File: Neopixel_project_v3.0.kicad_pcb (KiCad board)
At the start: 2 copper layers, 50 x 50 mm, 64 parts, among them J1 Conn_01x03_Pin, J2 Conn_01x02_Pin, Q1 MMBT3904, Q2 MMBT3904, Q3 MMBT3904, Q4 MMBT3904, Q5 DO3407B, Q6 DO3407B, Q7 DO3407B, Q8 DO3407B, SW1 TS-1088-AR02016, SW2 TS-1088-AR02016, U1 ESP8685H4, U2 AL8843, U3 TD1469, U4 USBLC6-4SC6, Y1 Crystal_GND24

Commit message: pcb finished
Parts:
- moved SW1 40.0 mm to (215.7, 127.2)
- moved R10 38.4 mm to (217.4, 124.8)
- moved SW2 35.2 mm to (200.8, 118.5), turned to 0 degrees
- moved C12 32.4 mm to (221.8, 130.5), turned to -90 degrees
- moved C11 31.1 mm to (205.5, 118.2)
- moved R3 27.7 mm to (202.0, 123.8), turned to -90 degrees
- moved R1 23.9 mm to (199.8, 123.7), turned to -90 degrees
- moved C18 22.2 mm to (214.3, 148.2), turned to 180 degrees
- moved C4 22.2 mm to (216.8, 149.2), turned to 0 degrees
- moved R9 21.8 mm to (214.3, 123.2), turned to 0 degrees
- moved Y1 21.7 mm to (214.3, 145.6), turned to 90 degrees
- moved R12 21.6 mm to (210.7, 124.2), turned to 180 degrees
- moved C17 21.6 mm to (214.5, 143.0), turned to 0 degrees
- moved AE1 21.5 mm to (218.8, 145.4), turned to -90 degrees
- moved J1 20.0 mm to (210.8, 121.0), turned to -90 degrees
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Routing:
- net CTRL: track 0.00 -> 58.5 mm, vias 0 -> 2
- net 3v3: track 36.4 -> 81.3 mm, vias 0 -> 11
- net PWM_B: track 0.00 -> 39.3 mm, vias 0 -> 2
- net PWM_G: track 0.00 -> 33.0 mm, vias 0 -> 2
- net PWM_W: track 0.00 -> 31.8 mm, vias 0 -> 2
- net CHIP_EN: track 0.00 -> 31.3 mm, vias 0 -> 2
- net GND: track 25.9 -> 55.7 mm, vias 10 -> 18
- net USB_D+: track 0.00 -> 26.6 mm
- net USB_D-: track 0.00 -> 24.2 mm
- net PWM_R: track 0.00 -> 22.2 mm, vias 0 -> 2
- net BOOT: track 0.00 -> 20.6 mm, vias 0 -> 2
- net Net-(U1A-GPIO2): track 0.00 -> 14.2 mm, vias 0 -> 2
- net OSC_N: track 0.00 -> 13.7 mm
- net Net-(U1A-GPIO8): track 0.00 -> 11.4 mm, vias 0 -> 2
- net Net-(Q2-C): track 4.91 -> 11.7 mm
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- added copper zone on F.Cu, net 3v3
- removed copper zone on F.Cu, net GND
- removed copper zone on F.Cu, net LNA_IN
- removed copper zone on F.Cu, net Net-(AE1-A)

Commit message: pcb and 3d models finished
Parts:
- removed J2: Conn_01x02_Pin, Connector_AMASS:AMASS_XT30UPB-M_1x02_P5.0mm_Vertical
- added J3: Screw_Terminal_01x02, TerminalBlock_Phoenix:TerminalBlock_Phoenix_MPT-0,5-2-2.54_1x02_P2.54mm_Horizontal, F.Cu at (195.5, 122.7)
- moved D5 0.40 mm to (186.0, 149.1)
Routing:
- net GND: track 55.7 -> 53.2 mm, vias 18 -> 17
- net PWM_G: track 33.0 -> 32.2 mm

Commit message: added bom.csv and buch of other changes
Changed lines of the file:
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@@
 		(tags "SOT TO_SOT_SMD")
 		(property "Reference" "Q4"
-			(at 0 -2.4 180)
+			(at -0.1125 -0.05 180)
 			(layer "F.SilkS")
 			(effects
@@
 		(tags "SOT TO_SOT_SMD")
 		(property "Reference" "Q8"
-			(at 0 -2.4 0)
+			(at -0.1 -0.3 0)
 			(layer "F.SilkS")
 			(effects
@@
 		(tags "Diode SMA (DO-214AC)")
 		(property "Reference" "D5"
-			(at 0 -2.5 180)
+			(at 0.025 -0.1 180)
 			(layer "F.SilkS")
 			(effects
@@
 		(tags "resistor")
 		(property "Reference" "R7"
-			(at 0 -1.82 90)
+			(at -0.1375 -0.1 90)
 			(layer "F.SilkS")
 			(effects
@@
 		(tags "resistor")
 		(property "Reference" "R15"
-			(at 0 -1.43 270)
+			(at 0 0.05 270)
 			(layer "F.SilkS")
 			(effects
@@
 		(tags "smd inductor dlg-0504")
 		(property "Reference" "L1"
-			(at 0 -3.7 180)
+			(at 0 -0.05 180)
 			(layer "F.SilkS")
 			(effects
@@
 		(tags "capacitor electrolytic")
 		(property "Reference" "C2"
-			(at 0 -4.35 360)
+			(at -0.05 0 360)
 			(layer "F.SilkS")
 			(effects
@@
 		(layer "User.1")
 	)
-	(gr_circle
-		(center 201 141)
-		(end 228.5 141)
-		(stroke
-			(width 0.1)
-			(type default)
-		)
-		(fill none)
-		(layer "User.2")
-	)
 	(dimension

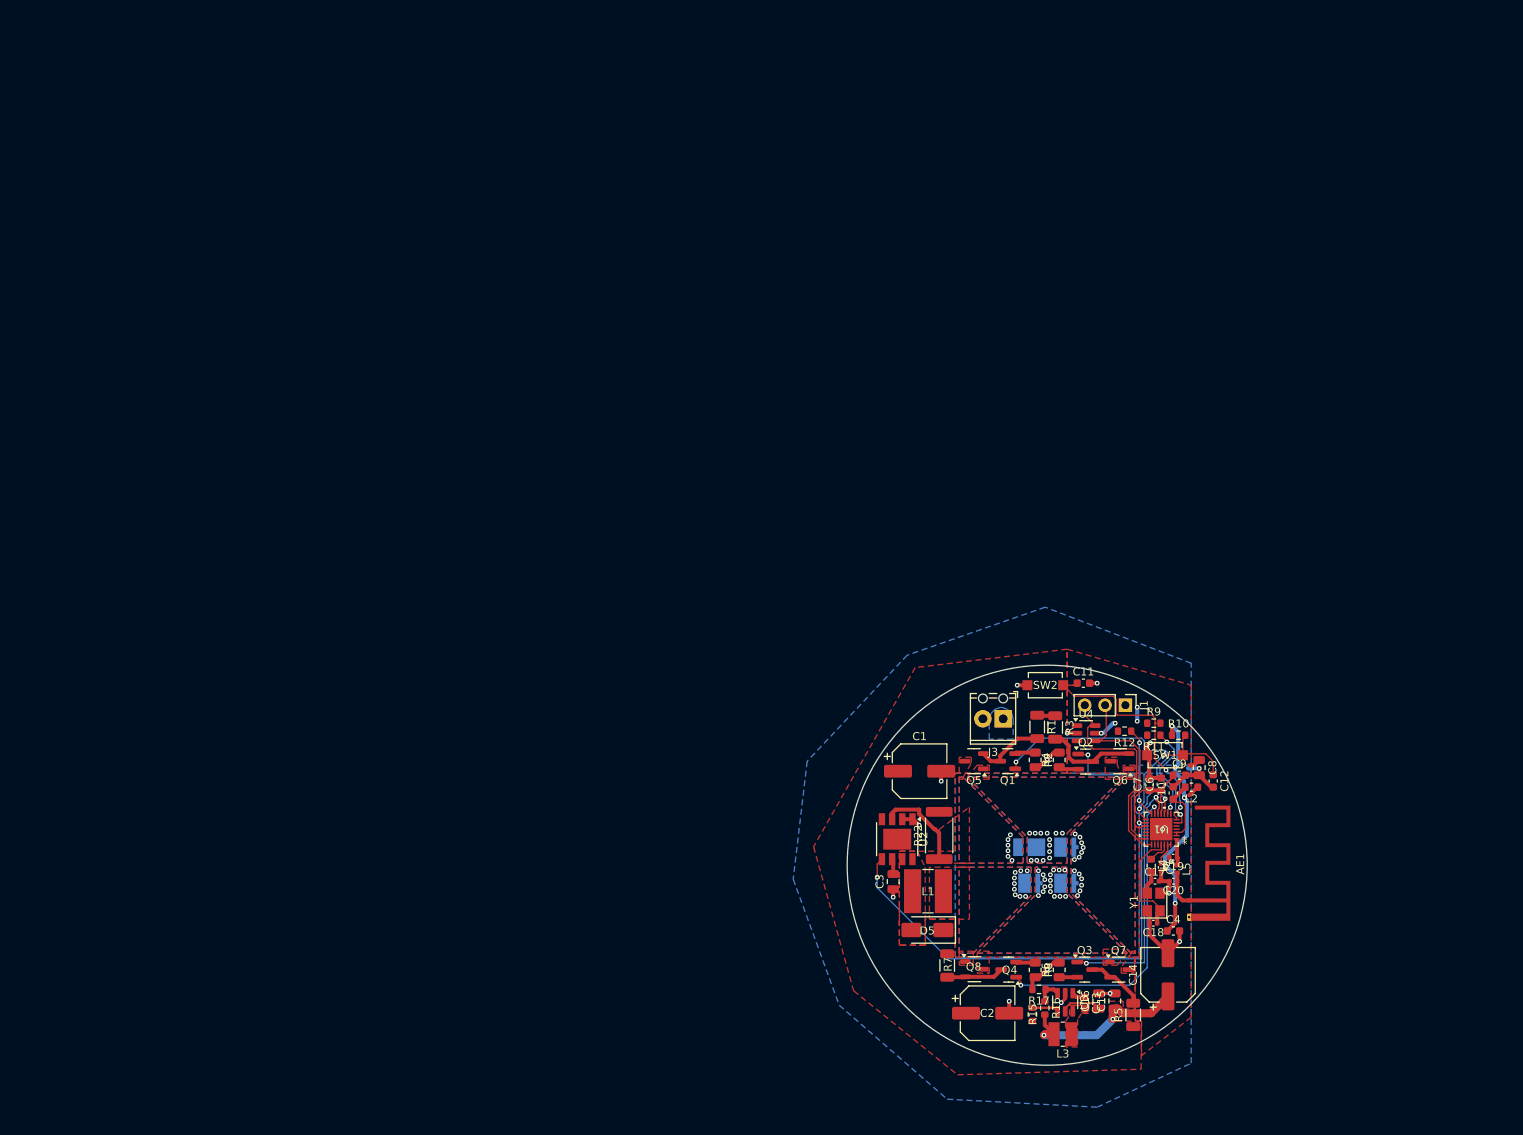
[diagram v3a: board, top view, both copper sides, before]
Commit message: silkscreen removed and layout printed
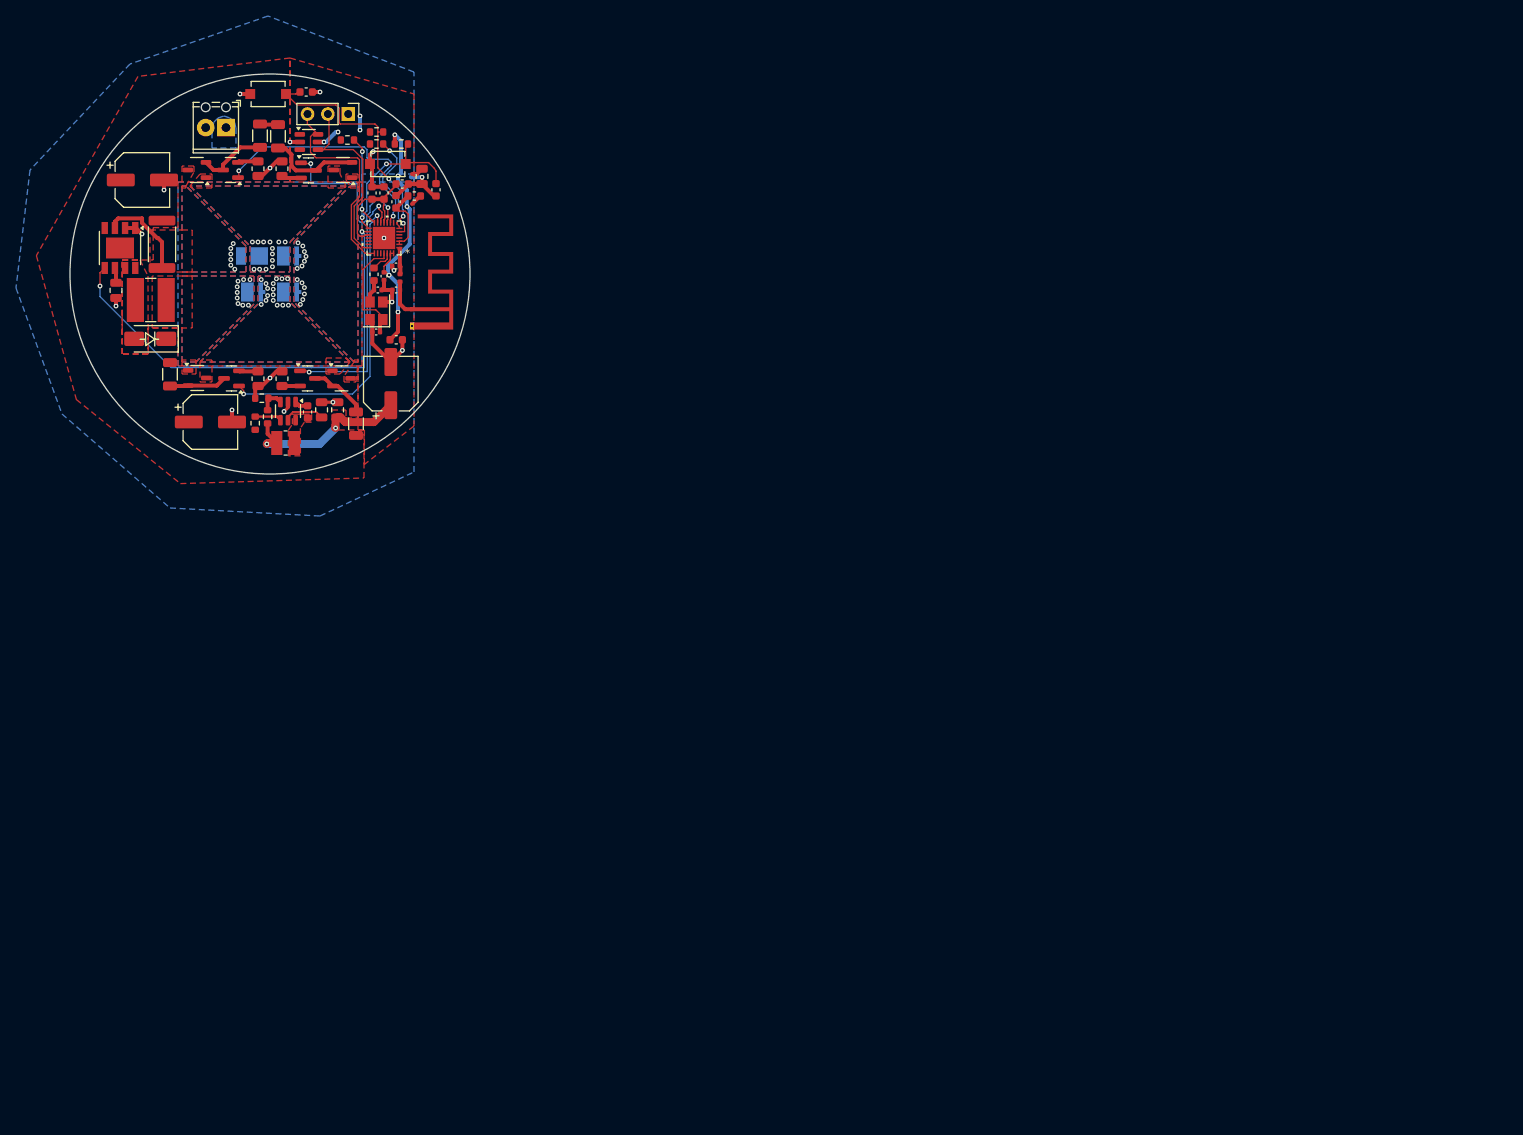
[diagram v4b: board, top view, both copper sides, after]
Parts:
- moved AE1 122.1 mm to (121.6, 71.5)
- moved C1 122.1 mm to (87.9, 55.4)
- moved C10 122.1 mm to (119.6, 58.1)
- moved C11 122.1 mm to (108.4, 44.4)
- moved C12 122.1 mm to (124.6, 56.6)
- moved C18 122.1 mm to (117.1, 74.3)
- moved C19 122.1 mm to (119.6, 66.1)
- moved C2 122.1 mm to (96.4, 85.6)
- moved C20 122.1 mm to (119.6, 69.1)
- moved C3 122.1 mm to (84.6, 69.2)
- moved C4 122.1 mm to (119.6, 75.3)
- moved C5 122.1 mm to (118.1, 67.4)
- moved C6 122.1 mm to (118.1, 57.0)
- moved C7 122.1 mm to (116.6, 57.0)
- moved C8 122.1 mm to (122.8, 54.9)
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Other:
- rule pad_to_mask_clearance: 0 -> 0.05
- board text added: "Neopixel v3.0"

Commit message: added gerber files
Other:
- rule pad_to_mask_clearance: 0.05 -> 0
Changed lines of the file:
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@@
 			(dielectric_constraints no)
 		)
-		(pad_to_mask_clearance 0.05)
+		(pad_to_mask_clearance 0)
 		(allow_soldermask_bridges_in_footprints no)
 		(pcbplotparams
@@
 			(outputformat 1)
 			(mirror no)
-			(drillshape 1)
+			(drillshape 0)
 			(scaleselection 1)
-			(outputdirectory "")
+			(outputdirectory "gerber/")
 		)
 	)
@@
 	)
 	(segment
+		(start 108.578339 79.2)
+		(end 108.744124 79.365785)
+		(width 0.2)
+		(layer "F.Cu")
+		(net 30)
+	)
+	(segment
 		(start 117.45 58.6)
 		(end 117.45 58.966116)
@@
 	)
 	(segment
-		(start 108.578339 79.2)
-		(end 107.6 79.2)
-		(width 0.15)
+		(start 107.6 79.2)
+		(end 108.578339 79.2)
+		(width 0.2)
 		(layer "F.Cu")
 		(net 30)
@@
 		(width 0.15)
 		(layer "F.Cu")
-		(net 30)
-	)
-	(segment
-		(start 108.744124 79.365785)
-		(end 108.578339 79.2)
-		(width 0.15)
-		(layer "F.Cu")

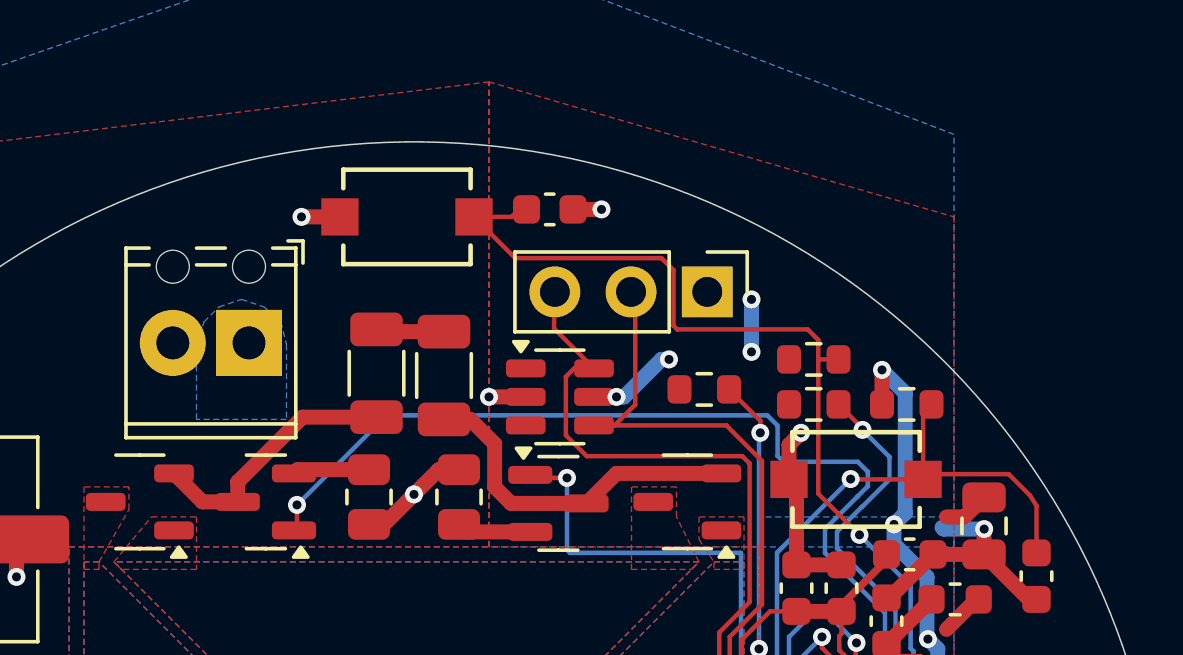
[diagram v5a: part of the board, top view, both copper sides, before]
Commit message: updated render and silkscreen
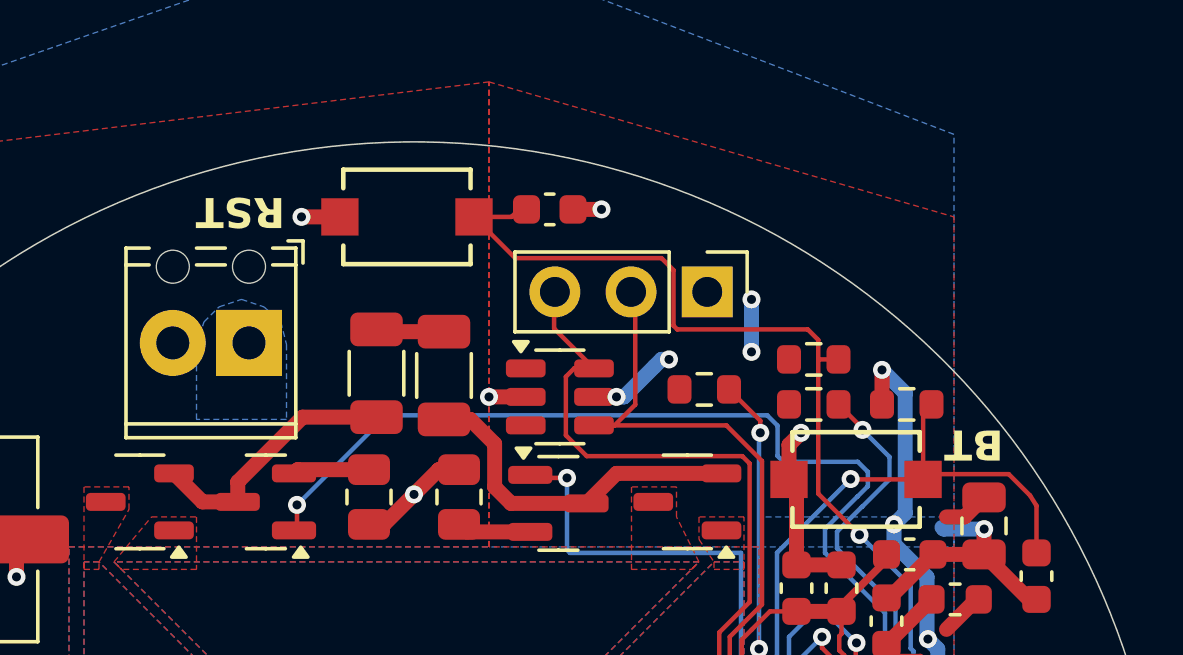
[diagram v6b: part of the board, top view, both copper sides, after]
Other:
- board text added: "BT"
- board text added: "RST"
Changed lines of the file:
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@@
+		)
+	)
+	(gr_text "RST"
+		(at 99.55 43.85 180)
+		(layer "F.SilkS")
+		(effects
+			(font
+				(size 1 1)
+				(thickness 0.2)
+				(bold yes)
+			)
+			(justify left bottom)
+		)
+	)
+	(gr_text "BT"
+		(at 123.5 51.6 180)
+		(layer "F.SilkS")
+		(effects
+			(font
+				(size 1 1)
+				(thickness 0.2)
+				(bold yes)
+			)
+			(justify left bottom)
 		)
 	)
